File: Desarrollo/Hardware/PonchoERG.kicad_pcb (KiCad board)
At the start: 2 copper layers, 86.4 x 80.5 mm, 91 parts, among them J1 Entradas Analógicas, J2 I/O's Multi Propósito, U1 TPD2E001, U10 ADS1299, U11 ADuM6401, U12 ADuM2401, U13 NCP1117ST33T3G, U14 OPA2376, U15 TPD2E001, U2 TPD2E001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

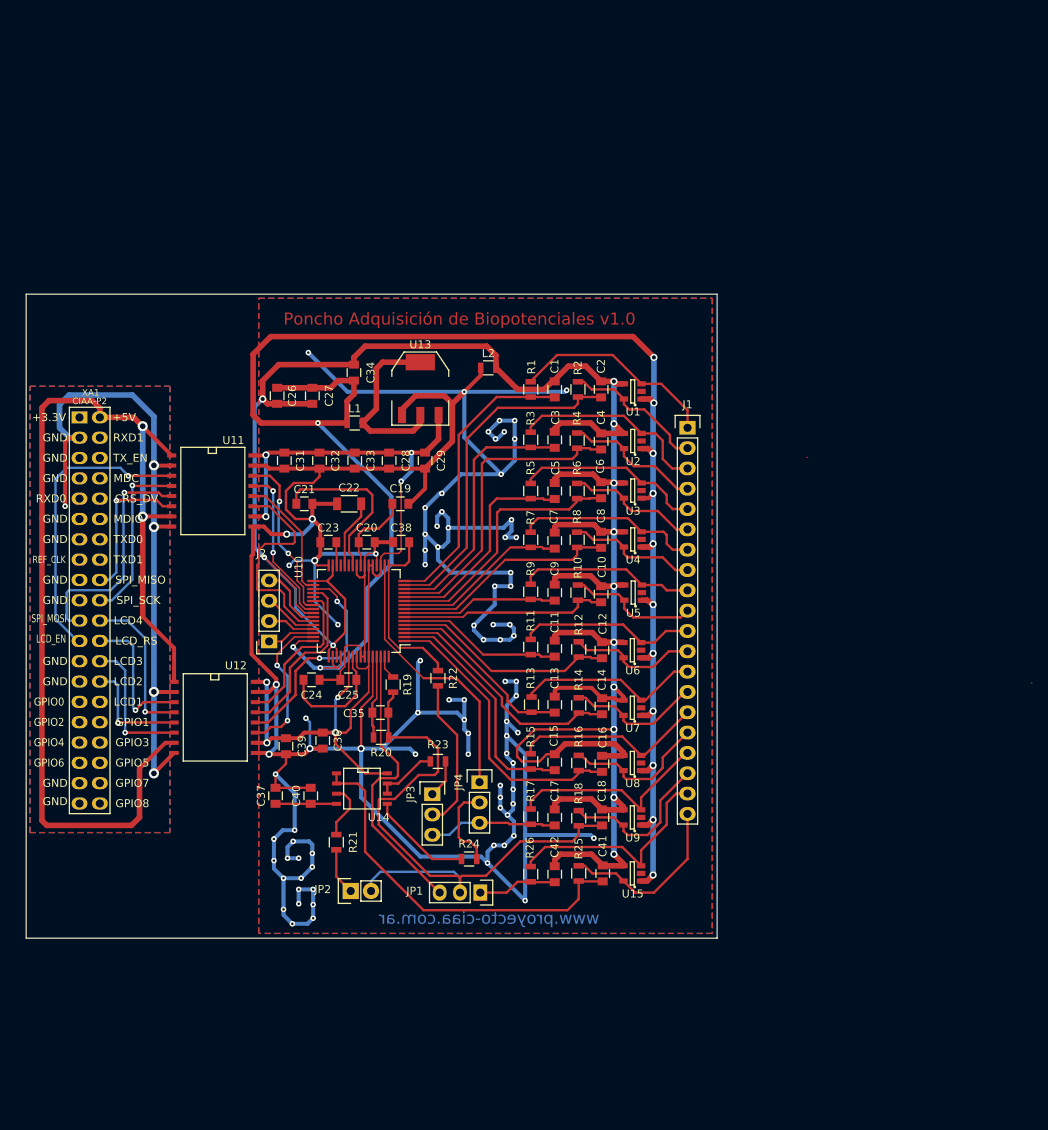
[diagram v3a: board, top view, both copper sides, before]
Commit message: Modificaciones basadas en nuevas revisiones. Se agregaron bypass en ADuMs. Inclusión de símbolos de "PONCHO" y "OPEN HARDWARE". Algunos cambios estéticos de pistas y otros funcionales. Unificación de vías. Extensión de capas de cobre en sector de aislación. Mejora de stitching. Quedaron revisiones pendientes que serán consultadas.
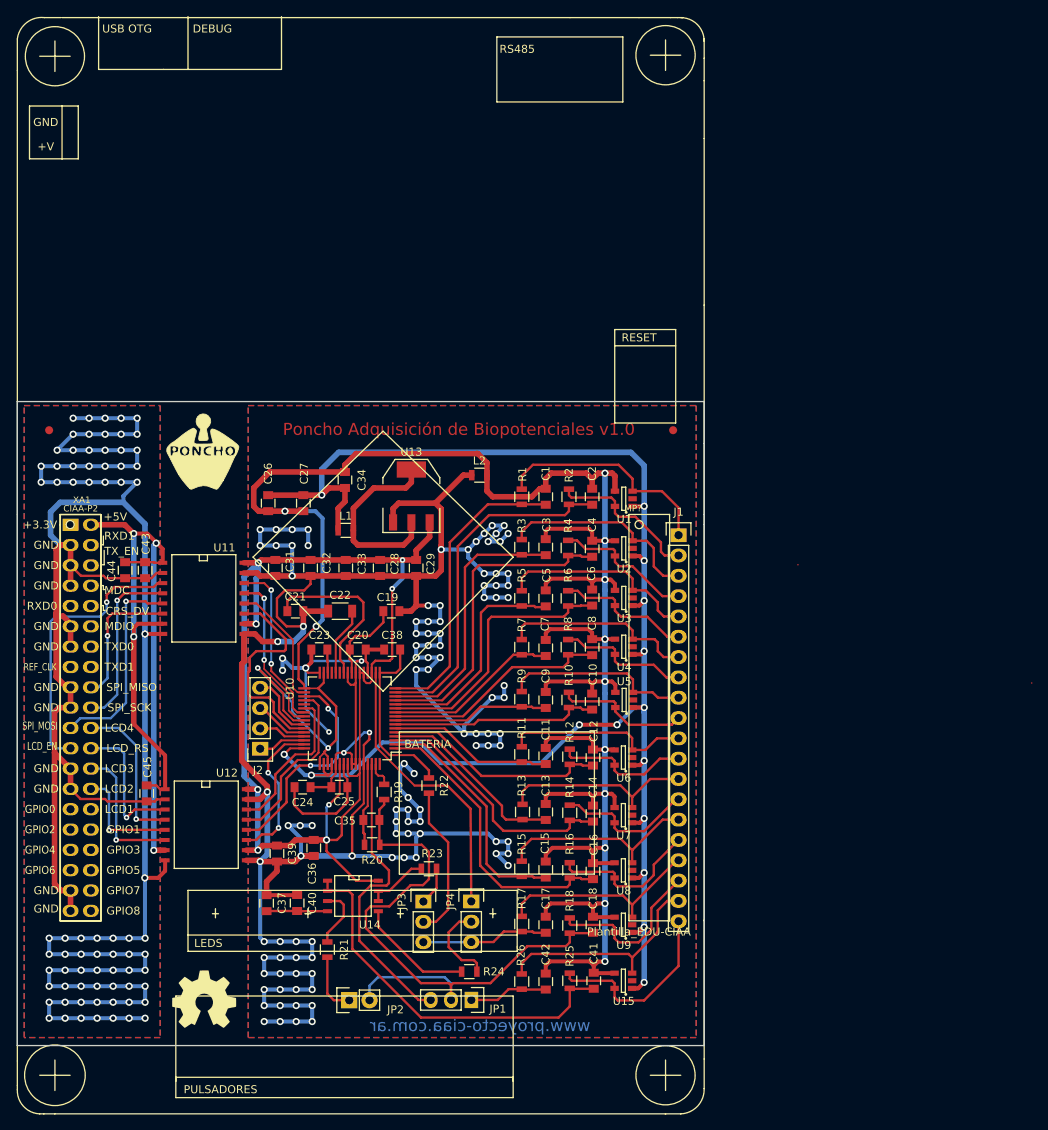
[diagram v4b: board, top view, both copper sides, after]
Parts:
- added ?: Fiducial_1mm_Dia_2.54mm_Outer_CopperTop, Fiducials:Fiducial_1mm_Dia_2.54mm_Outer_CopperTop, F.Cu at (104.0, 71.5)
- added ?: Fiducial_1mm_Dia_2.54mm_Outer_CopperTop, Fiducials:Fiducial_1mm_Dia_2.54mm_Outer_CopperTop, F.Cu at (182.0, 71.5)
- added C43: 0.1uF, Capacitors_SMD:C_0805, F.Cu at (116.0, 89.0)
- added C44: 10uF, Capacitors_SMD:C_0805, F.Cu at (113.5, 89.0)
- added C45: 0.1uF, Capacitors_SMD:C_0805, F.Cu at (116.2, 116.9)
- added G***: LOGO, Poncho_Esqueleto:Logo_Poncho, F.Cu at (123.2, 74.2)
- added G101: Logo_OSHWA, Poncho_Esqueleto:Logo_OSHWA, F.Cu at (123.4, 142.6)
- added MP?: Plantilla_EDU-CIAA, Poncho_Esqueleto:Plantilla_EDU-CIAA, F.Cu at (177.8, 83.3)
- XA1: footprint Poncho_Esqueleto:Conn_Poncho_Izquierdo -> Conn_Poncho_Izquierdo
- moved JP4 14.9 mm to (156.8, 130.4)
- moved R24 14.1 mm to (156.5, 139.2)
- moved JP2 13.7 mm to (141.5, 142.8)
- moved C40 13.5 mm to (135.0, 130.6)
- moved C10 13.5 mm to (171.9, 105.4)
- moved C12 13.5 mm to (172.0, 112.4)
- moved C14 13.5 mm to (172.0, 119.4)
- moved C16 13.5 mm to (172.0, 126.6)
- moved C19 13.5 mm to (146.8, 94.1)
- moved C21 13.5 mm to (134.8, 94.1)
- moved C22 13.5 mm to (140.4, 94.1)
- moved C23 13.5 mm to (137.8, 98.9)
- moved C24 13.5 mm to (135.7, 116.1)
- moved C25 13.5 mm to (140.3, 116.1)
- moved C26 13.5 mm to (131.4, 80.6)
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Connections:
- net Earth renamed DGND
- XA1 pad 45: (no net) -> /AISLACIÓN/GND_NISO
- XA1 pad 47: (no net) -> /AISLACIÓN/GND_NISO
- XA1 pad 51: (no net) -> /AISLACIÓN/GND_NISO
- XA1 pad 53: (no net) -> /AISLACIÓN/GND_NISO
- XA1 pad 57: (no net) -> /AISLACIÓN/GND_NISO
- XA1 pad 59: (no net) -> /AISLACIÓN/GND_NISO
- XA1 pad 65: (no net) -> /AISLACIÓN/GND_NISO
- XA1 pad 67: (no net) -> /AISLACIÓN/GND_NISO
- XA1 pad 77: (no net) -> /AISLACIÓN/GND_NISO
- XA1 pad 79: (no net) -> /AISLACIÓN/GND_NISO
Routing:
- net /AISLACIÓN/GND_NISO: track 86.2 -> 314.2 mm, vias 5 -> 74
- net GNDA: track 521.8 -> 430.6 mm, vias 88 -> 114
- net /AISLACIÓN/+5V_NISO: track 134.5 -> 98.3 mm, vias 2 -> 4
- net +5V: track 122.9 -> 152.6 mm
- net +3V3: track 221.4 -> 201.9 mm, vias 14 -> 15
- net Net-(U11-Pad5): track 29.6 -> 25.6 mm
- net Net-(J1-Pad1): track 26.1 -> 28.4 mm
- net Net-(J1-Pad5): track 23.6 -> 25.5 mm
- net Net-(R24-Pad2): track 12.9 -> 14.7 mm
- net Net-(U11-Pad3): track 36.9 -> 35.1 mm
- net Net-(JP2-Pad1): track 5.90 -> 7.64 mm
- net Net-(U11-Pad6): track 18.8 -> 17.2 mm
- net Net-(J1-Pad9): track 22.0 -> 23.5 mm
- net Net-(J1-Pad15): track 24.3 -> 25.8 mm
- net Net-(JP4-Pad1): track 34.5 -> 36.0 mm
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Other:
- board size 86.4 x 80.5 mm -> 85.9 x 80.5 mm
- board text added: "1+ 1- 2+ 2- 3+ 3- 4+ 4- 5+ 5- 6+ 6- 7+ 7- 8+ 8- IN_REF BIAS_DRV BIAS_ELEC BIAS_SHD"

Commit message: Actualización final con todas las revisiones corregidas. Realizar revisión FINAL.
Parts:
- removed ? (x2): Fiducial_1mm_Dia_2.54mm_Outer_CopperTop, Fiducials:Fiducial_1mm_Dia_2.54mm_Outer_CopperTop
- removed G***: LOGO, Poncho_Esqueleto:Logo_Poncho
- removed G101: Logo_OSHWA, Poncho_Esqueleto:Logo_OSHWA
- added FD1: Fiducial, Fiducials:Fiducial_1mm_Dia_2.54mm_Outer_CopperTop, F.Cu at (136.0, 73.5)
- added FD2: Fiducial, Fiducials:Fiducial_1mm_Dia_2.54mm_Outer_CopperTop, F.Cu at (172.0, 73.5)
- added FD3: Fiducial, Fiducials:Fiducial_1mm_Dia_2.54mm_Outer_CopperTop, F.Cu at (136.0, 144.0)
- added FD4: Fiducial, Fiducials:Fiducial_1mm_Dia_2.54mm_Outer_CopperTop, F.Cu at (172.0, 144.0)
- added FD5: Fiducial, Fiducials:Fiducial_1mm_Dia_2.54mm_Outer_CopperTop, B.Cu at (136.0, 73.5)
- added FD6: Fiducial, Fiducials:Fiducial_1mm_Dia_2.54mm_Outer_CopperTop, B.Cu at (172.0, 73.5)
- added FD7: Fiducial, Fiducials:Fiducial_1mm_Dia_2.54mm_Outer_CopperTop, B.Cu at (136.0, 144.0)
- added FD8: Fiducial, Fiducials:Fiducial_1mm_Dia_2.54mm_Outer_CopperTop, B.Cu at (172.0, 144.0)
- added FD9: Fiducial, Fiducials:Fiducial_1mm_Dia_2.54mm_Outer_CopperTop, F.Cu at (150.5, 101.5)
- added MH1: PCB_HOLE, Connect:1pin, F.Cu at (182.0, 71.5)
- added MH2: PCB_HOLE, Connect:1pin, F.Cu at (182.0, 144.5)
- added MH3: PCB_HOLE, Connect:1pin, F.Cu at (103.5, 71.0)
- added MH4: PCB_HOLE, Connect:1pin, F.Cu at (103.5, 144.5)
- J2: value I/O's Multi Propósito -> IOs Multipropósito; footprint Pin_Headers:Pin_Header_Straight_1x04 -> Pin_Headers:Pin_Header_Straight_1x05
- XA1: footprint Conn_Poncho_Izquierdo -> Poncho_Esqueleto:Conn_Poncho_Izquierdo
- moved J2 2.00 mm to (130.8, 113.3)
- moved C24 1.74 mm to (136.4, 117.7)
- moved MP? 0.05 mm to (177.8, 83.3)
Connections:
- J2 pad 1: Net-(J2-Pad1) -> DGND
- U10 pad 42: Net-(J2-Pad4) -> Net-(J2-Pad5)
- U10 pad 44: Net-(J2-Pad3) -> Net-(J2-Pad4)
- U10 pad 45: Net-(J2-Pad2) -> Net-(J2-Pad3)
- U10 pad 46: Net-(J2-Pad1) -> Net-(J2-Pad2)
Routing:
- net GNDA: track 430.6 -> 404.1 mm, vias 114 -> 102
- net DGND: track 303.8 -> 294.7 mm
- net Net-(J2-Pad5): track 0.00 -> 8.66 mm
- net Net-(J2-Pad1): track 5.93 -> 0.00 mm
- net /AISLACIÓN/GND_NISO: track 314.2 -> 309.0 mm, vias 74 -> 71
- net +3V3: track 201.9 -> 198.6 mm
- net Net-(C24-Pad1): track 14.9 -> 13.0 mm
- net Net-(J2-Pad4): track 8.51 -> 6.66 mm
- net /ADS1299/BIAS_DRV: track 78.9 -> 77.1 mm
- net /ADS1299/START: track 19.5 -> 21.1 mm
- net /ADS1299/RESET: track 22.6 -> 24.1 mm
- net /ADS1299/DRDY/: track 18.9 -> 17.9 mm
- net Net-(J2-Pad3): track 6.76 -> 5.71 mm
- net /ADS1299/CS/: track 21.3 -> 22.3 mm
- net /ADS1299/MISO: track 26.9 -> 26.3 mm
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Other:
- board text added: "BIAS_DRV"
- board text added: "BIAS_ELEC"
- board text added: "BUFFER"
- board text added: "Buffer_IN"
- board text added: "DGND"
- board text added: "GPIO_1"
- board text added: "GPIO_2"
- board text added: "GPIO_3"
- board text added: "GPIO_4"
- board text added: "IN_REF"
- board text added: "IN_REF_Buffer"
- board text added: "OFF"
- board text added: "ON"
- board text added: "SHIELD"
- board text added: "SRB1"
- board text added: "SRB2"
- board text added: "Zona_Corte"

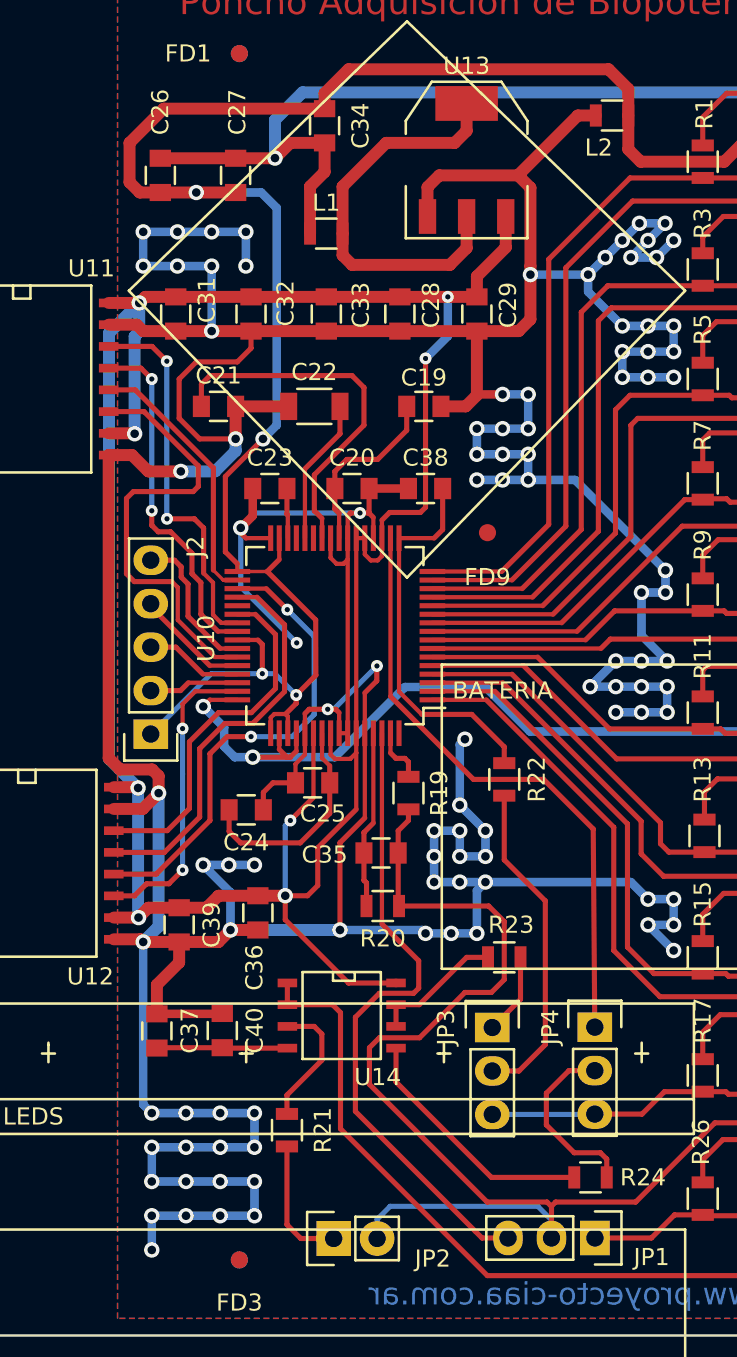
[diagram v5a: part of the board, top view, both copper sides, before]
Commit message: Nueva actualización. Intercambio de tierras GNDA por DGND en hoja esquemático "Aislación". Ídem en hoja de "Protección". Además se hizo visible el nombre de la tierra digital DGND que no figuraba. Revisión FINAL. Cambios estéticos en ubicación de algunas pistas del PCB.
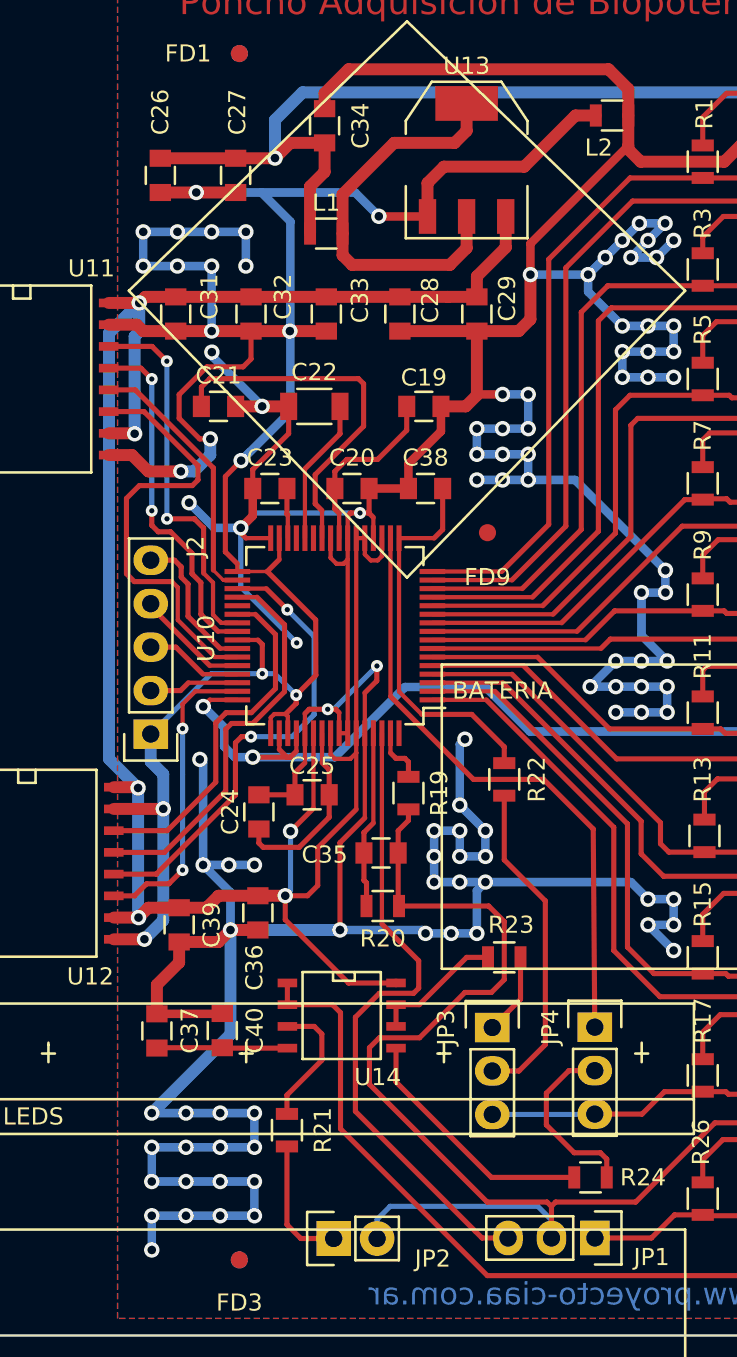
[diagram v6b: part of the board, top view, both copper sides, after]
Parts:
- moved C24 0.75 mm to (137.1, 117.8), turned to 90 degrees
- moved C25 0.70 mm to (140.2, 116.8)
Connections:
- C1 pad 2: DGND -> GNDA
- C10 pad 2: DGND -> GNDA
- C11 pad 2: DGND -> GNDA
- C12 pad 2: DGND -> GNDA
- C13 pad 2: DGND -> GNDA
- C14 pad 2: DGND -> GNDA
- C15 pad 2: DGND -> GNDA
- C16 pad 2: DGND -> GNDA
- C17 pad 2: DGND -> GNDA
- C18 pad 2: DGND -> GNDA
- C2 pad 2: DGND -> GNDA
- C3 pad 2: DGND -> GNDA
- C31 pad 2: GNDA -> DGND
- C32 pad 2: GNDA -> DGND
- C33 pad 2: GNDA -> DGND
- C34 pad 2: DGND -> GNDA
- C4 pad 2: DGND -> GNDA
- C41 pad 2: DGND -> GNDA
- C42 pad 2: DGND -> GNDA
- C5 pad 2: DGND -> GNDA
- C6 pad 2: DGND -> GNDA
- C7 pad 2: DGND -> GNDA
- C8 pad 2: DGND -> GNDA
- C9 pad 2: DGND -> GNDA
- L2 pad 1: DGND -> GNDA
- L2 pad 2: GNDA -> DGND
- U1 pad 4: DGND -> GNDA
- U11 pad 15: GNDA -> DGND
- U11 pad 9: GNDA -> DGND
- U12 pad 15: GNDA -> DGND
- U12 pad 9: GNDA -> DGND
- U13 pad 1: GNDA -> DGND
- U15 pad 4: DGND -> GNDA
- U2 pad 4: DGND -> GNDA
- U3 pad 4: DGND -> GNDA
- U4 pad 4: DGND -> GNDA
- U5 pad 4: DGND -> GNDA
- U6 pad 4: DGND -> GNDA
- U7 pad 4: DGND -> GNDA
- U8 pad 4: DGND -> GNDA
- U9 pad 4: DGND -> GNDA
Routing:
- net DGND: track 294.7 -> 154.2 mm, vias 14 -> 19
- net GNDA: track 404.1 -> 540.8 mm, vias 102 -> 103
- net +5V: track 152.6 -> 135.8 mm, vias 8 -> 6
- net Net-(C24-Pad1): track 13.0 -> 10.8 mm

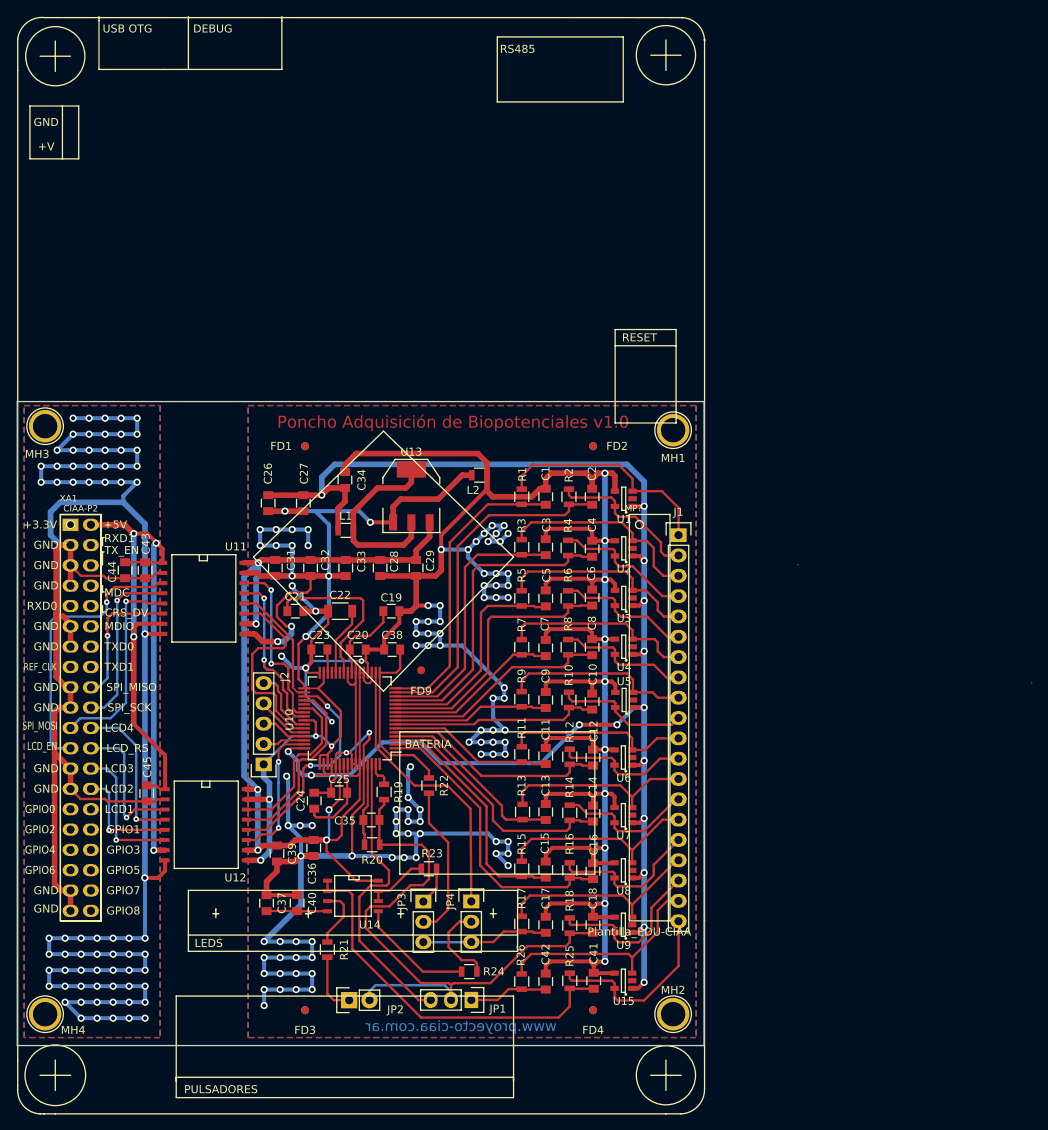
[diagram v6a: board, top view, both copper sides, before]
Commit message: Separación de planos de tierras DGND y GNDA. PCB Finalizado. REVISAR
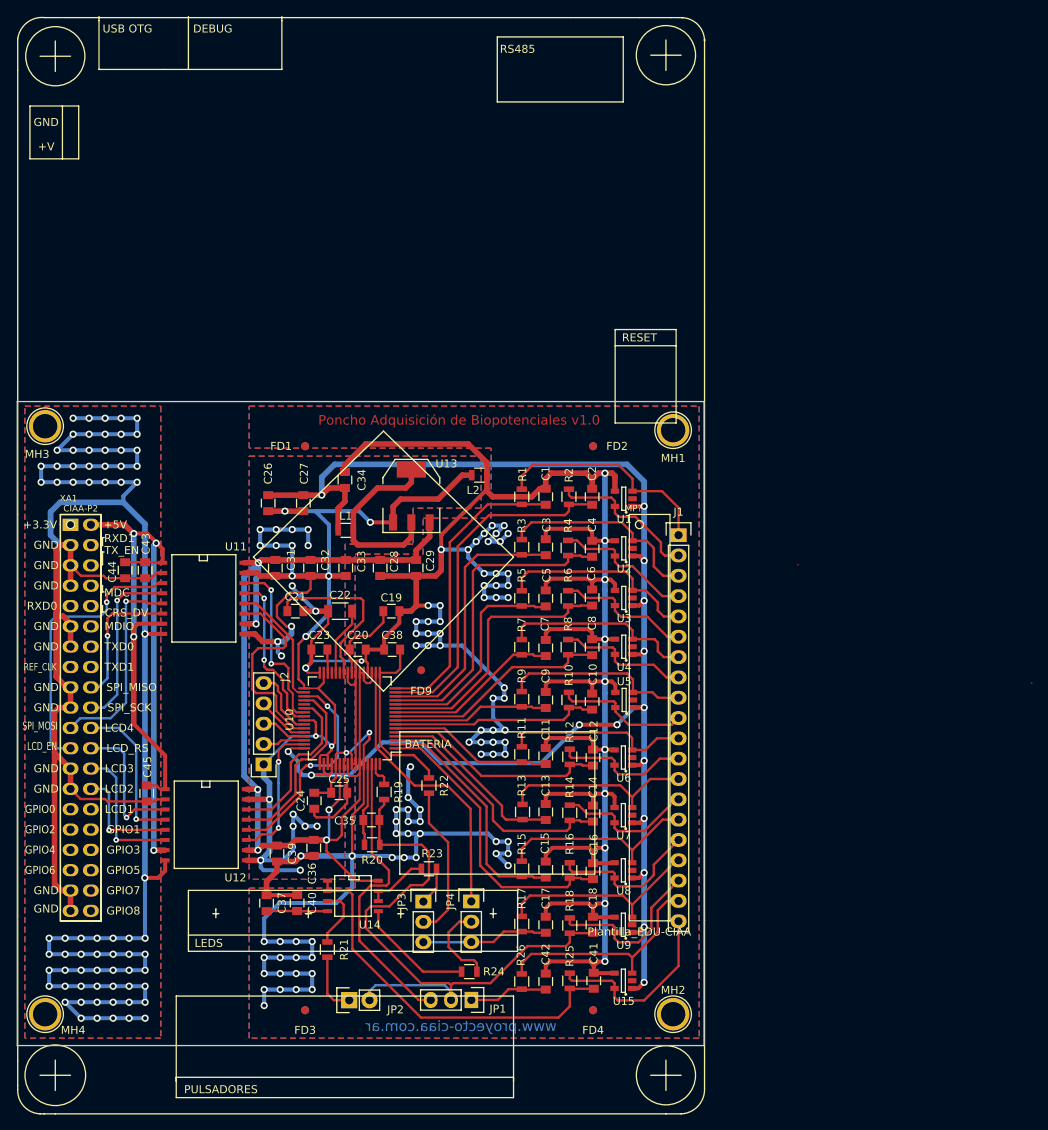
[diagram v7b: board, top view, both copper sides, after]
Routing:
- net DGND: track 154.2 -> 174.2 mm, vias 19 -> 25
- net GNDA: track 540.8 -> 523.2 mm, vias 103 -> 97
- added copper zone on B.Cu, net DGND
- added copper zone on F.Cu, net DGND
